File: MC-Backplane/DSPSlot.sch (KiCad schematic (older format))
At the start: 1 part, among them J40 374472

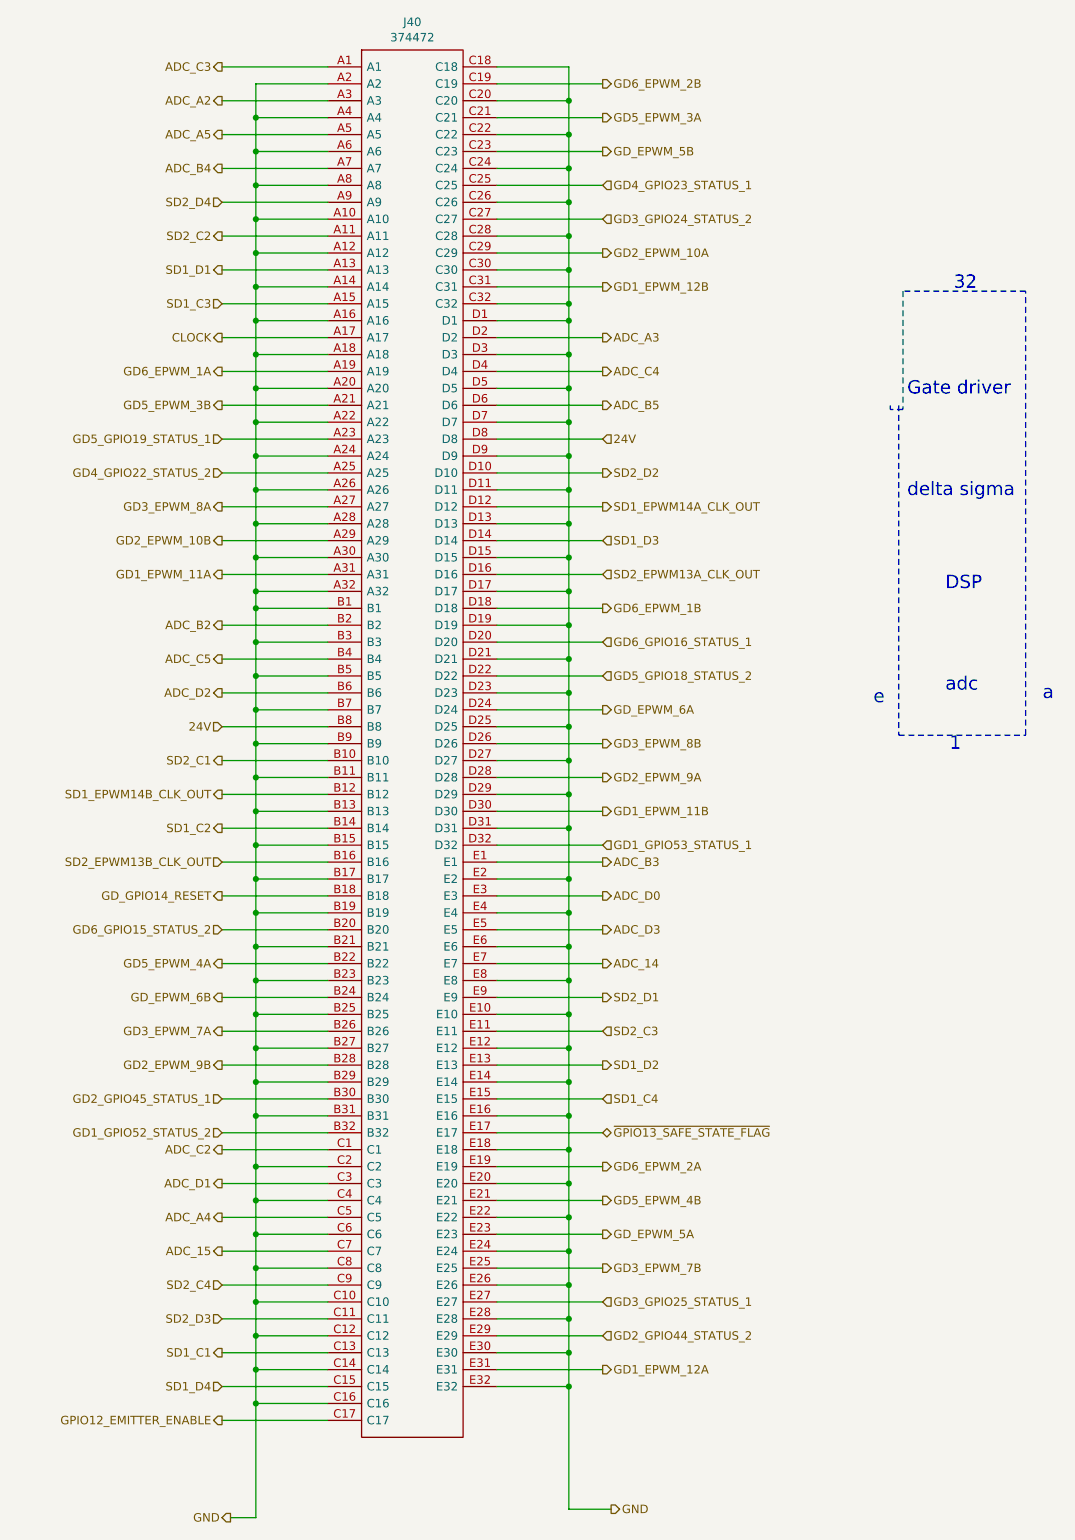
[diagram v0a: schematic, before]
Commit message: schematic reorg and layout begins
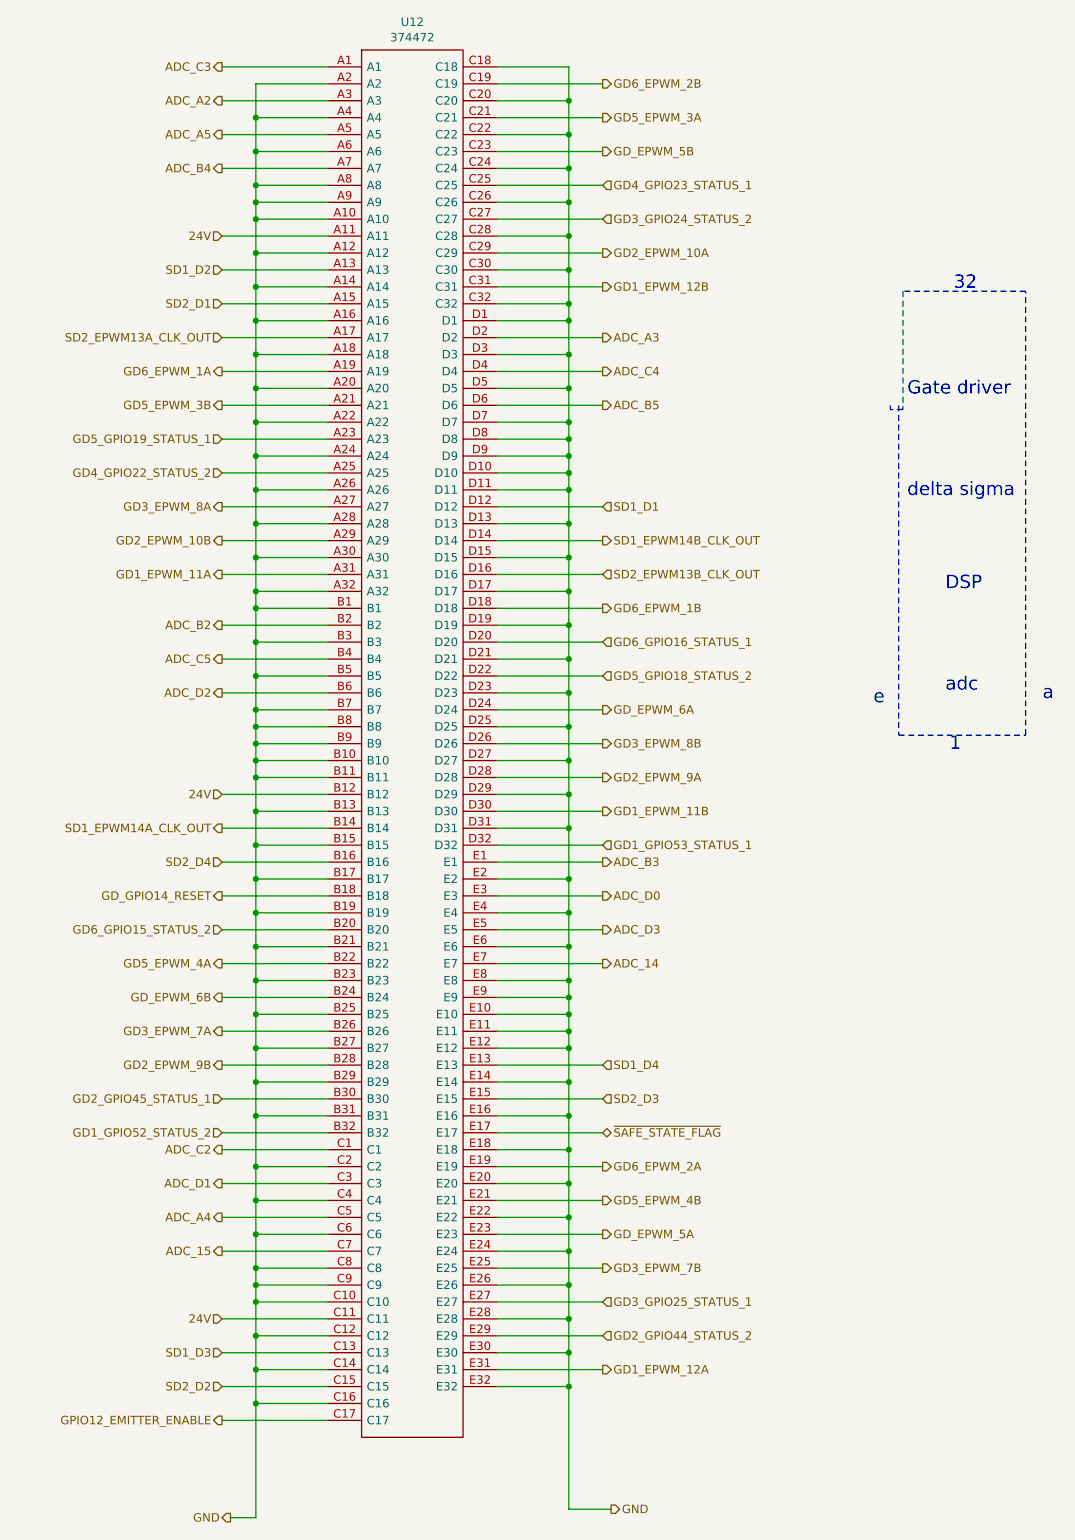
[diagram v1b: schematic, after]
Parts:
- renumbered J40 to U12
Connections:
- net CLOCK is gone; now on net SD2_EPWM13A_CLK_OUT: U12.A17
- net SD1_C1 is gone; now on net SD1_D3: U12.C13
- net SD1_C2 is gone; now on net SD1_EPWM14A_CLK_OUT: U12.B14
- net SD1_C3 is gone; now on net SD2_D1: U12.A15
- net SD1_C4 is gone; now on net SD2_D3: U12.E15
- net SD2_C1 is gone; now on net GND: U12.B10
- net SD2_C2 is gone; now on net 24V: U12.A11
- net SD2_C3 is gone; now on net GND: U12.E11
- net SD2_C4 is gone; now on net GND: U12.C9
- net 24V: now also U12.B12, U12.C11; no longer U12.B8, U12.D8
- net GND: now also U12.A9, U12.B8, U12.D10, U12.D8, U12.E9
- net SD1_D1: now also U12.D12; no longer U12.A13
- net SD1_D2: now also U12.A13; no longer U12.E13
- net SD1_D3: no longer U12.D14
- net SD1_D4: now also U12.E13; no longer U12.C15
- net SD1_EPWM14A_CLK_OUT: no longer U12.D12
- net SD1_EPWM14B_CLK_OUT: now also U12.D14; no longer U12.B12
- net SD2_D1: no longer U12.E9
- net SD2_D2: now also U12.C15; no longer U12.D10
- net SD2_D3: no longer U12.C11
- net SD2_D4: now also U12.B16; no longer U12.A9
- net SD2_EPWM13A_CLK_OUT: no longer U12.D16
- net SD2_EPWM13B_CLK_OUT: now also U12.D16; no longer U12.B16
- net ~GPIO13_SAFE_STATE_FLAG~ renamed ~SAFE_STATE_FLAG~

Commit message: placement done- tracks started
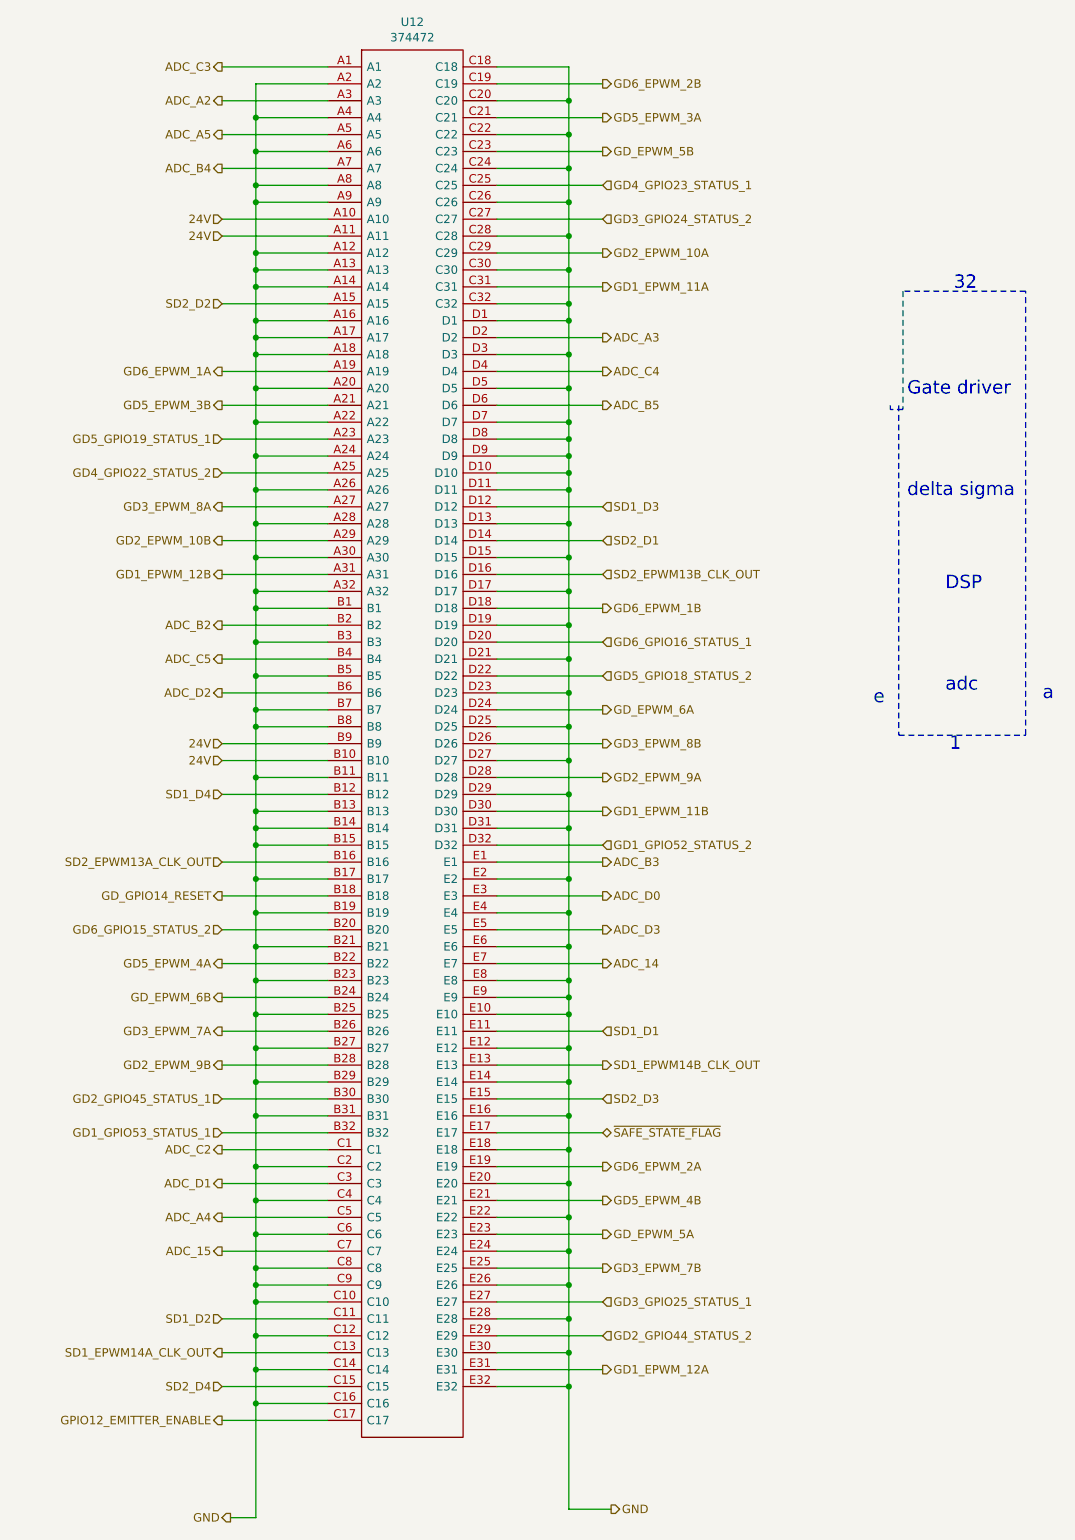
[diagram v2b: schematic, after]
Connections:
- net 24V: now also U12.A10, U12.B10, U12.B9; no longer U12.B12, U12.C11
- net GD1_EPWM_11A: now also U12.C31; no longer U12.A31
- net GD1_EPWM_12B: now also U12.A31; no longer U12.C31
- net GD1_GPIO52_STATUS_2: now also U12.D32; no longer U12.B32
- net GD1_GPIO53_STATUS_1: now also U12.B32; no longer U12.D32
- net GND: now also U12.A13, U12.A17, U12.B14; no longer U12.A10, U12.B10, U12.B9, U12.E11
- net SD1_D1: now also U12.E11; no longer U12.D12
- net SD1_D2: now also U12.C11; no longer U12.A13
- net SD1_D3: now also U12.D12; no longer U12.C13
- net SD1_D4: now also U12.B12; no longer U12.E13
- net SD1_EPWM14A_CLK_OUT: now also U12.C13; no longer U12.B14
- net SD1_EPWM14B_CLK_OUT: now also U12.E13; no longer U12.D14
- net SD2_D1: now also U12.D14; no longer U12.A15
- net SD2_D2: now also U12.A15; no longer U12.C15
- net SD2_D4: now also U12.C15; no longer U12.B16
- net SD2_EPWM13A_CLK_OUT: now also U12.B16; no longer U12.A17
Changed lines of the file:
@@
 $Descr A4 8268 11693 portrait
 encoding utf-8
-Sheet 12 14
+Sheet 14 14
 Title ""
 Date ""
@@
 Wire Wire Line
 	2950 7500 2950 7800
-Connection ~ 2950 5300
 Connection ~ 2950 5100
 Wire Wire Line
 	2950 5100 2950 5200
-Wire Wire Line
-	2950 2200 2950 2400
-Connection ~ 2950 2200
 Wire Wire Line
 	2950 2000 2950 2100
@@
 Wire Wire Line
 	4800 2700 4800 2800
-Wire Wire Line
-	4800 6900 4800 7000
 Connection ~ 4800 6900
 Wire Wire Line
@@
 Connection ~ 2950 5900
 Wire Wire Line
-	2950 5700 2950 5900
+	2950 5700 2950 5800
 Connection ~ 2950 5700
-Wire Wire Line
-	2950 5500 2950 5700
-Connection ~ 2950 5500
-Wire Wire Line
-	2950 5300 2950 5400
 Wire Wire Line
 	2950 4000 2950 4200
@@
 Connection ~ 2950 3000
 Wire Wire Line
-	2950 2800 2950 3000
+	2950 2800 2950 2900
 Connection ~ 2950 2800
 Wire Wire Line
@@
 Connection ~ 2950 2600
 Wire Wire Line
-	2950 2400 2950 2600
+	2950 2400 2950 2500
 Connection ~ 2950 2400
 Text HLabel 2800 9875 0    50   Output ~ 0
@@
 	4375 7200 5000 7200
 Wire Wire Line
-	4375 7000 4800 7000
-Wire Wire Line
 	4375 6800 4800 6800
 Wire Wire Line
@@
 	2950 5700 3375 5700
 Wire Wire Line
-	2950 5500 3375 5500
-Wire Wire Line
-	2950 5300 3375 5300
-Wire Wire Line
 	2950 5100 3375 5100
 Wire Wire Line
@@
 	2950 2400 3375 2400
 Wire Wire Line
-	2950 2200 3375 2200
-Wire Wire Line
 	2950 1800 3375 1800
 Wire Wire Line
@@
 	2750 6000 3375 6000
 Wire Wire Line
-	2750 5800 3375 5800
+	2950 5800 3375 5800
 Wire Wire Line
 	2750 5600 3375 5600
 Wire Wire Line
-	2950 5400 3375 5400
-Wire Wire Line
 	2950 5200 3375 5200
 Wire Wire Line
@@
 	2750 3100 3375 3100
 Wire Wire Line
-	2750 2900 3375 2900
-Wire Wire Line
-	2750 2500 3375 2500
+	2950 2900 3375 2900
+Wire Wire Line
+	2950 2500 3375 2500
 Wire Wire Line
 	2750 2300 3375 2300
@@
 Text HLabel 5000 8200 2    50   Output ~ 0
 GD_EPWM_5A
-Text HLabel 5000 4100 2    50   Output ~ 0
+Text HLabel 5000 7200 2    50   Output ~ 0
 SD1_EPWM14B_CLK_OUT
-Text HLabel 2750 5800 0    50   Output ~ 0
+Text HLabel 2750 8900 0    50   Output ~ 0
 SD1_EPWM14A_CLK_OUT
 Text HLabel 5000 2200 2    50   Input ~ 0
@@
 Text HLabel 5000 5500 2    50   Output ~ 0
 GD2_EPWM_9A
-Text HLabel 2750 7600 0    50   Input ~ 0
+Text HLabel 5000 5900 2    50   Input ~ 0
 GD1_GPIO52_STATUS_2
-Text HLabel 5000 2600 2    50   Output ~ 0
+Text HLabel 2750 4300 0    50   Output ~ 0
 GD1_EPWM_12B
 Text HLabel 5000 9000 2    50   Output ~ 0
 GD1_EPWM_12A
-Text HLabel 5000 5900 2    50   Input ~ 0
+Text HLabel 2750 7600 0    50   Input ~ 0
 GD1_GPIO53_STATUS_1
 Text HLabel 5000 5700 2    50   Output ~ 0
 GD1_EPWM_11B
-Text HLabel 2750 4300 0    50   Output ~ 0
+Text HLabel 5000 2600 2    50   Output ~ 0
 GD1_EPWM_11A
 Text HLabel 5000 4300 2    50   Input ~ 0
 SD2_EPWM13B_CLK_OUT
-Text HLabel 2750 2900 0    50   Input ~ 0
+Text HLabel 2750 6000 0    50   Input ~ 0
 SD2_EPWM13A_CLK_OUT
-Text HLabel 2750 5600 0    50   Input ~ 0
-24V
 Text HLabel 5050 9825 2    50   Output ~ 0
 GND
@@
 Text HLabel 2750 9300 0    50   Output ~ 0
 GPIO12_EMITTER_ENABLE
+Text HLabel 5000 7000 2    50   Input ~ 0
+SD1_D1
 Text HLabel 5000 3900 2    50   Input ~ 0
-SD1_D1
-Text HLabel 5000 7200 2    50   Input ~ 0
+SD1_D3
+Text HLabel 2750 8700 0    50   Input ~ 0
+SD1_D2
+Text HLabel 5000 4100 2    50   Input ~ 0
+SD2_D1
+Text HLabel 2750 9100 0    50   Input ~ 0
+SD2_D4
+Text HLabel 2750 2700 0    50   Input ~ 0
+SD2_D2
+Connection ~ 2950 5200
+Connection ~ 2950 2100
+Connection ~ 4800 3500
+Wire Wire Line
+	4800 3500 4800 3600
+Connection ~ 4800 3700
+Wire Wire Line
+	4800 3700 4800 3600
+Connection ~ 4800 6800
+Wire Wire Line
+	4800 6800 4800 6900
+Wire Wire Line
+	2750 2700 3375 2700
+Connection ~ 2950 8500
+Wire Wire Line
+	2950 8500 2950 8600
+Wire Wire Line
+	4800 6900 4800 7100
+Wire Wire Line
+	4375 7000 5000 7000
+Connection ~ 2950 5800
+Wire Wire Line
+	2950 5800 2950 5900
+Wire Wire Line
+	2950 2100 2950 2400
+Text HLabel 2750 2200 0    50   Input ~ 0
+24V
+Wire Wire Line
+	2750 2200 3375 2200
+Text HLabel 2750 5300 0    50   Input ~ 0
+24V
+Wire Wire Line
+	2750 5300 3375 5300
+Text HLabel 2750 5400 0    50   Input ~ 0
+24V
+Wire Wire Line
+	2750 5400 3375 5400
+Connection ~ 2950 2500
+Wire Wire Line
+	2950 2500 2950 2600
+Connection ~ 2950 2900
+Wire Wire Line
+	2950 2900 2950 3000
+Text HLabel 2750 5600 0    50   Input ~ 0
 SD1_D4
-Text HLabel 2750 8900 0    50   Input ~ 0
-SD1_D3
-Text HLabel 2750 2500 0    50   Input ~ 0
-SD1_D2
-Text HLabel 2750 2700 0    50   Input ~ 0
-SD2_D1
-Text HLabel 2750 6000 0    50   Input ~ 0
-SD2_D4
 Text HLabel 5000 7400 2    50   Input ~ 0
 SD2_D3
-Text HLabel 2750 9100 0    50   Input ~ 0
-SD2_D2
-Text HLabel 2750 8700 0    50   Input ~ 0
-24V
-Connection ~ 2950 5200
-Wire Wire Line
-	2950 5200 2950 5300
-Connection ~ 2950 5400
-Wire Wire Line
-	2950 5400 2950 5500
-Connection ~ 2950 2100
-Wire Wire Line
-	2950 2100 2950 2200
-Connection ~ 4800 3500
-Wire Wire Line
-	4800 3500 4800 3600
-Connection ~ 4800 3700
-Wire Wire Line
-	4800 3700 4800 3600
-Connection ~ 4800 6800
-Wire Wire Line
-	4800 6800 4800 6900
-Connection ~ 4800 7000
-Wire Wire Line
-	4800 7000 4800 7100
-Wire Wire Line
-	2750 2700 3375 2700
-Connection ~ 2950 8500
-Wire Wire Line
-	2950 8500 2950 8600
+Wire Wire Line
+	2950 5200 2950 5500
+Wire Wire Line
+	3375 5500 2950 5500
+Connection ~ 2950 5500
+Wire Wire Line
+	2950 5500 2950 5700
 $EndSCHEMATC
